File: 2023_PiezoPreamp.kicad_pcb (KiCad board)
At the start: 4 copper layers, 68 x 35.5 mm, 73 parts, among them J101 6.3mm stereo, J102 6.3mm stereo, J201 Molex PicoBlade, J301 2.54mm header, J401 Spring Contact, U101 OPA145, U102 OPA145, U201 ZXMP3A17E6TA, U301 MMDT2222A-7-F

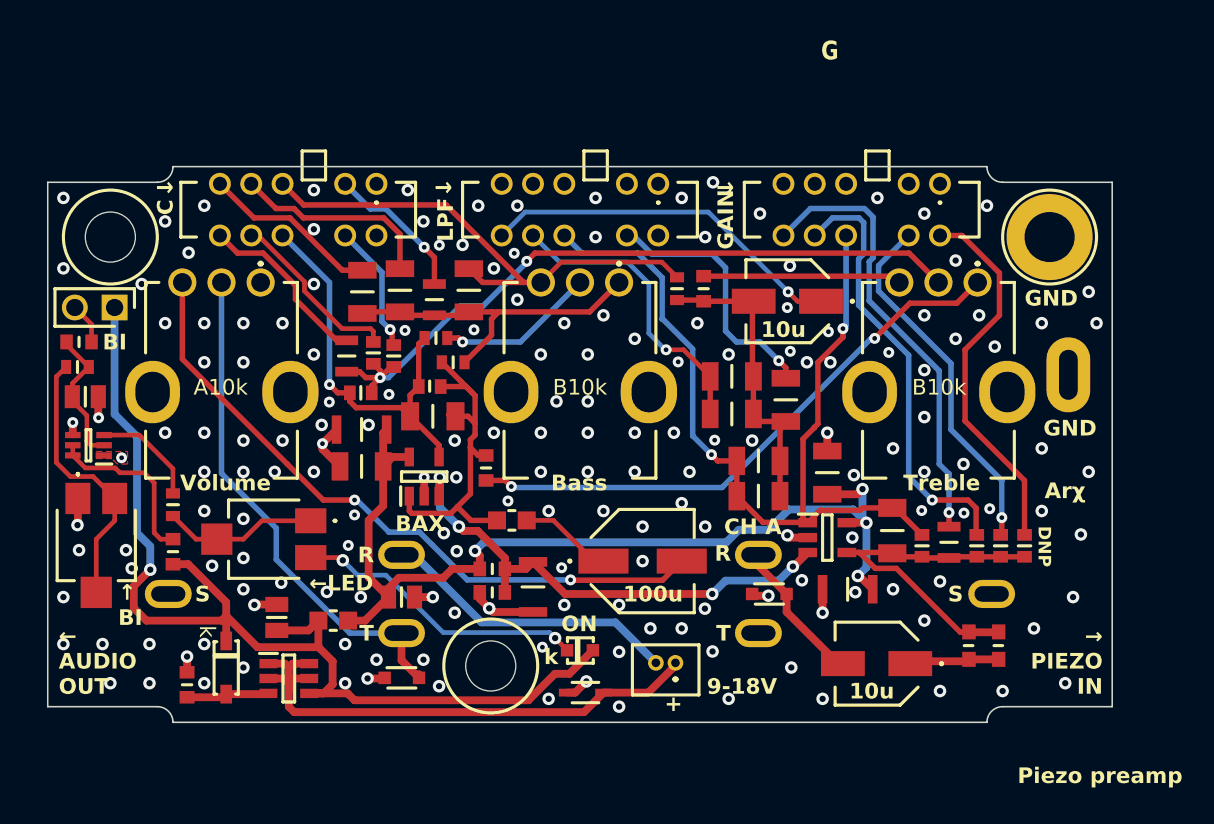
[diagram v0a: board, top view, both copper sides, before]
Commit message: resolving all violations of stitching vias
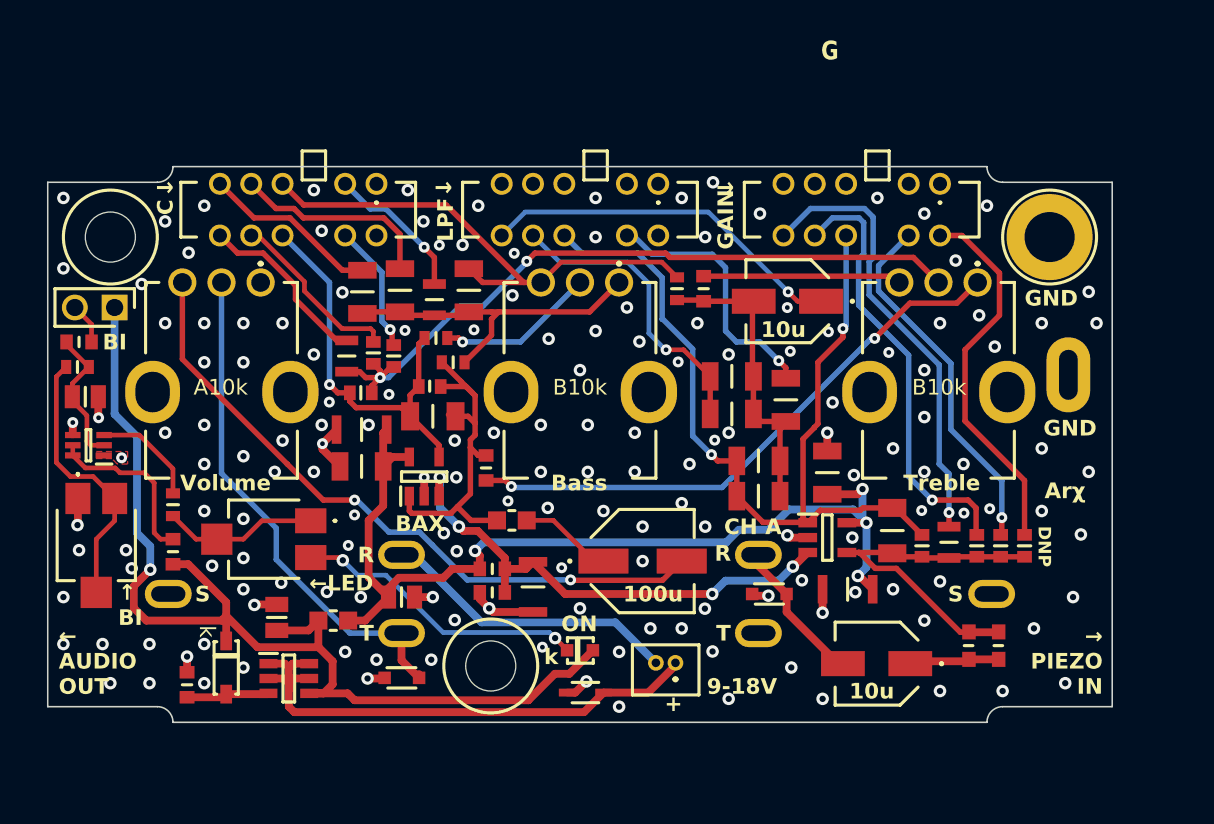
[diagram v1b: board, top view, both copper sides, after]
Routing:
- net GND: vias 177 -> 164
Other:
- board text removed: "Piezo preamp"

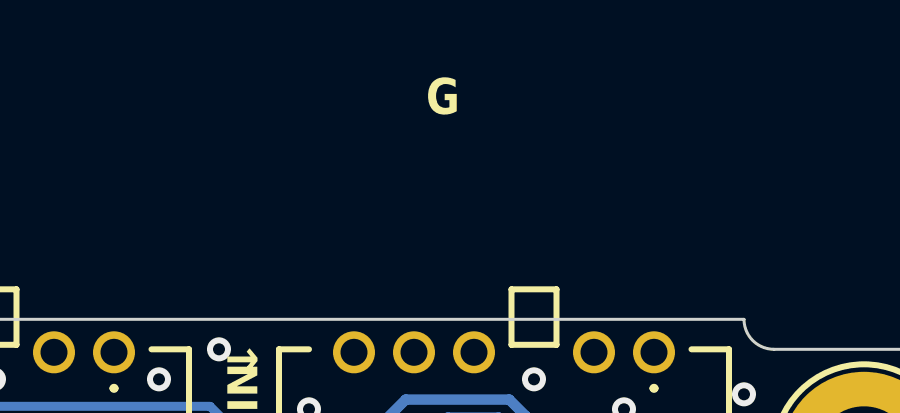
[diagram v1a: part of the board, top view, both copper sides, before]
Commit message: removing forggoten text
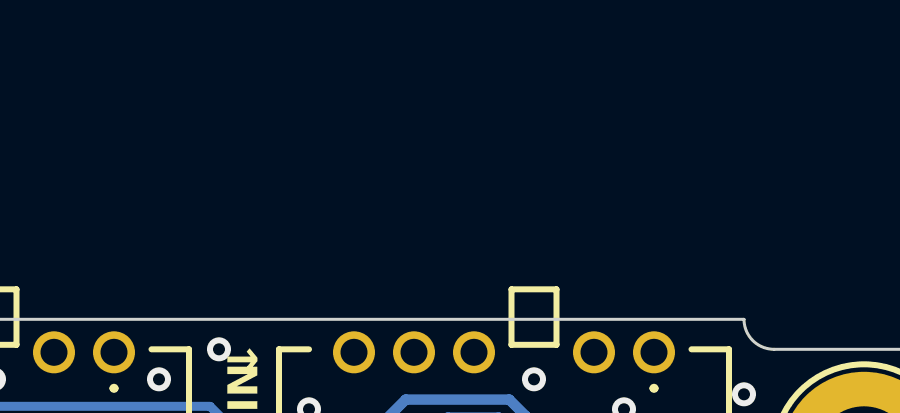
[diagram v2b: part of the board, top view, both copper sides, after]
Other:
- board text removed: "G"
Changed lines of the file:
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@@
     (effects (font (size 1 1) (thickness 0.2) bold) (justify left bottom))
-  )
-  (gr_text "G" (at 89.4 22.8) (layer "F.SilkS")
-    (effects (font (size 1.2 1) (thickness 0.2) bold) (justify left bottom))
   )
   (gr_text "DNP" (at 103.2 52.45 270) (layer "F.SilkS")

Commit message: final touches to board and schematic before manufacture / assembly
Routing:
- net /1-ChargeAmpAndEQ/CH_A_OUT: track 58.2 -> 57.3 mm
- net /1-ChargeAmpAndEQ/LPF_SW_6: track 23.9 -> 23.4 mm
- net GND: vias 164 -> 165
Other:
- board text added: "Arχ v2.0"
- board text added: "BAX↑"
- board text added: "BI↑"
- board text added: "CHA→"
- board text added: "JLCJLCJLCJLC"
- board text added: "L"
- board text added: "LOW"
- board text added: "NONE"
- board text added: "↑CENT"
- board text added: "↑GAIN"
- board text added: "↑LPF"
- board text added: "↖ BI"
- board text added: "↖LED"
- board text removed: "Arχ"
- board text removed: "BAX"
- board text removed: "BI"
- board text removed: "C"
- board text removed: "CH A"
- board text removed: "GAIN"
- board text removed: "LPF"
- board text removed: "←LED"
- board text removed: "↑ BI"
- board text removed: "→"

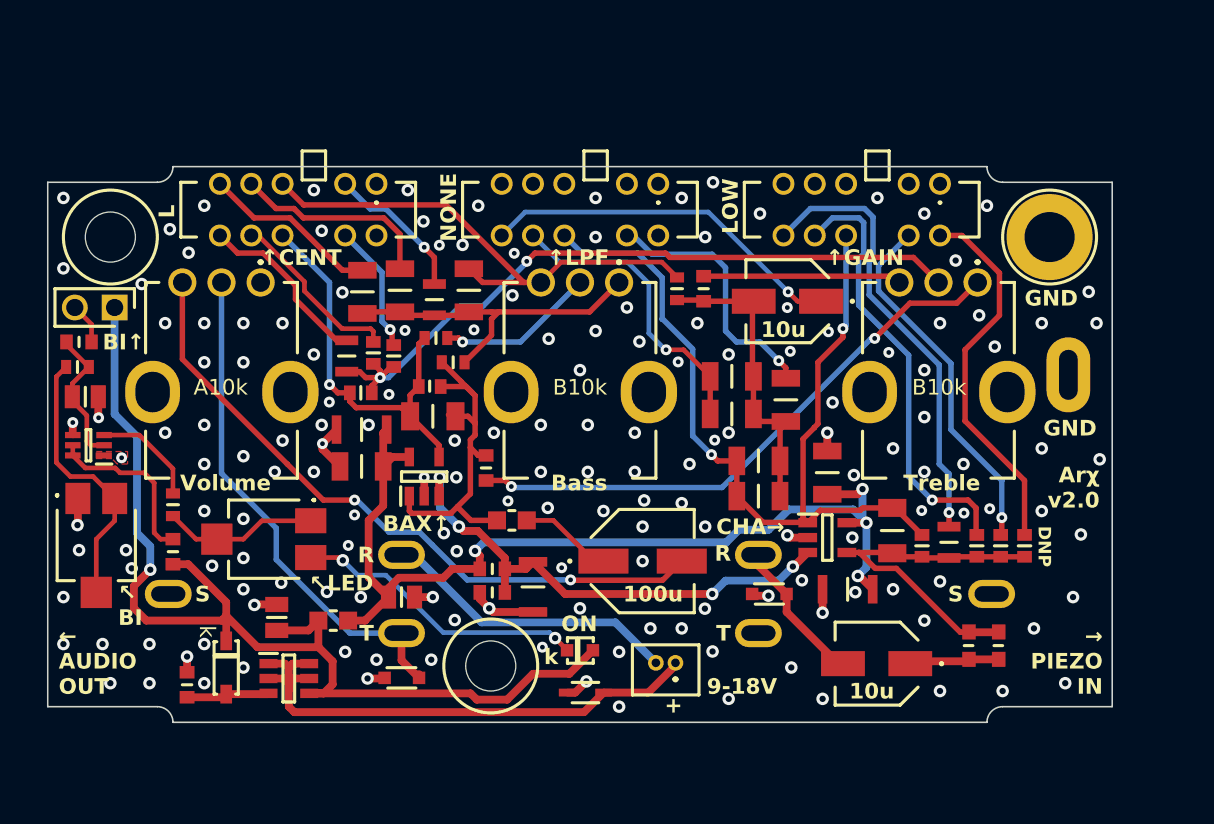
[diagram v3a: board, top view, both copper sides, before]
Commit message: fixing some of 0805 and 1206 land patterns so that they have enough soldering area (after JLC feedback)
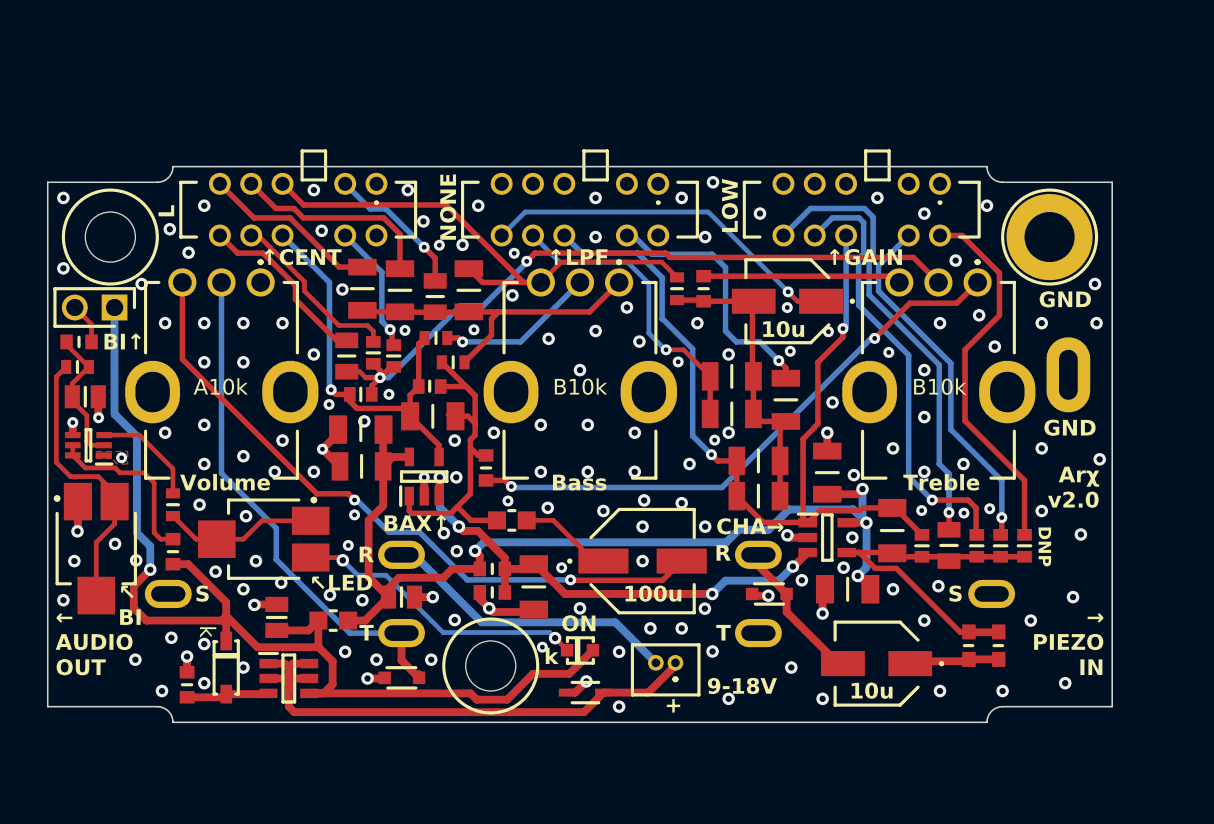
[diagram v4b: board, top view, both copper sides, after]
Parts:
- moved Cb104 0.21 mm to (64.8, 37.8)
- moved Cb102 0.20 mm to (60.1, 37.3)
- moved Cf102 0.20 mm to (97.6, 53.7)
- moved RV301 0.20 mm to (43.1, 53.9)
- moved Ct101 0.10 mm to (60.0, 44.0)
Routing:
- net GND: track 23.7 -> 24.0 mm, vias 165 -> 162

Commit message: PCB: few minor fixes, vias etc
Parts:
- D202: value DDZ12B-7 -> SOD3716X145N
- U201: value ZXMP3A17E6TA -> SOT95P285X140-6N
- U301: value MMDT2222A-7-F -> SOT65P210X110-6N
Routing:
- net Vbi: track 69.2 -> 61.0 mm
- net GND: vias 162 -> 175
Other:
- board text added: "Arχ v2.1"
- board text added: "↑ BI"
- board text added: "↑BI"
- board text removed: "Arχ v2.0"
- board text removed: "BI↑"
- board text removed: "↖ BI"

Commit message: updating the project and board (silkscreen mistake, was v2.0 instead of v2.1)
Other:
- board text added: "Piezo Preamp + EQ v2.1 12/2023 Arχ arx.wtf"
- board text removed: "Piezo Preamp + EQ v2.0 12/2023 Arχ arx.wtf"
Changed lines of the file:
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@@
     (effects (font (size 1 1) (thickness 0.2) bold) (justify left bottom mirror))
   )
-  (gr_text "Piezo Preamp + EQ \nv2.0 12/2023\nArχ\narx.wtf\n" (at 73.9 54.7) (layer "B.SilkS")
+  (gr_text "Piezo Preamp + EQ \nv2.1 12/2023\nArχ\narx.wtf\n" (at 73.9 54.7) (layer "B.SilkS")
     (effects (font (size 1.2 1) (thickness 0.2) bold) (justify bottom mirror))
   )

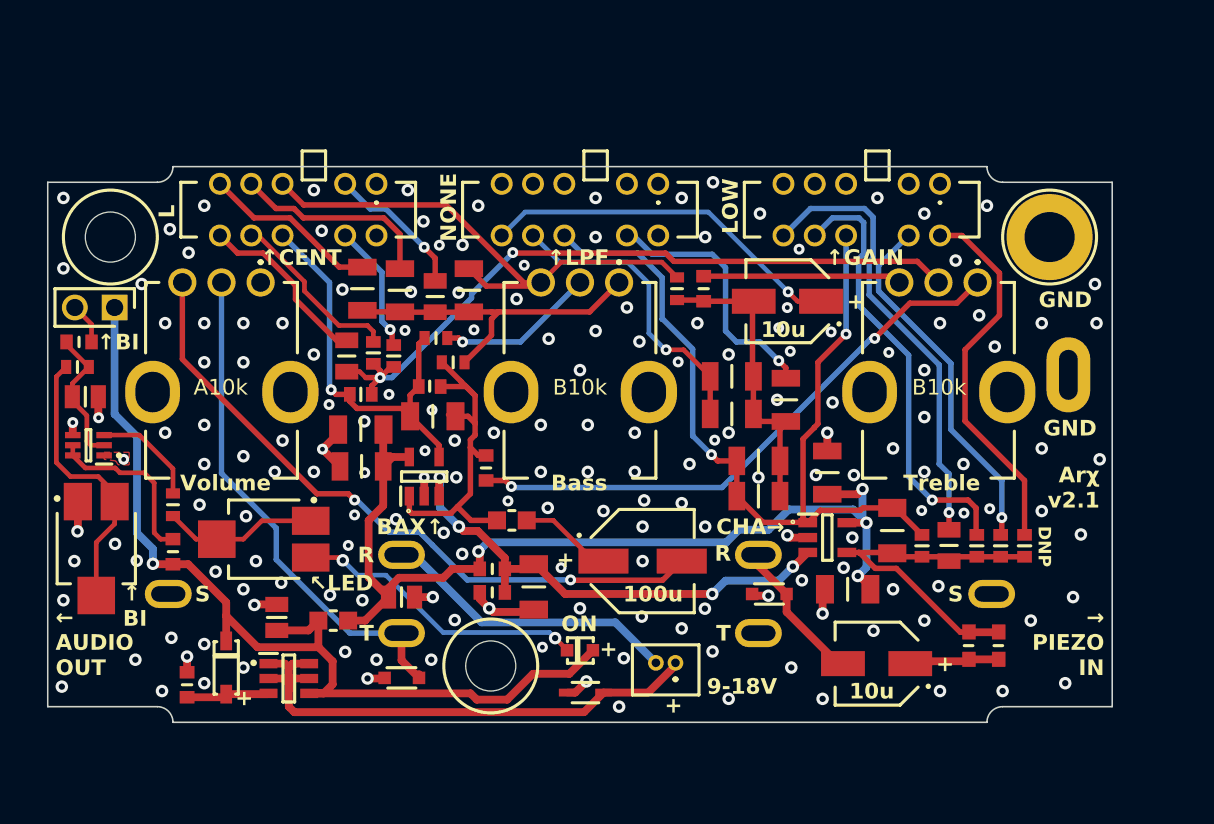
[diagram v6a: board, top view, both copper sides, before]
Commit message: v2.2: correcting pins of audio jacks - T and R were swapped. Fixing in schematic and PCB
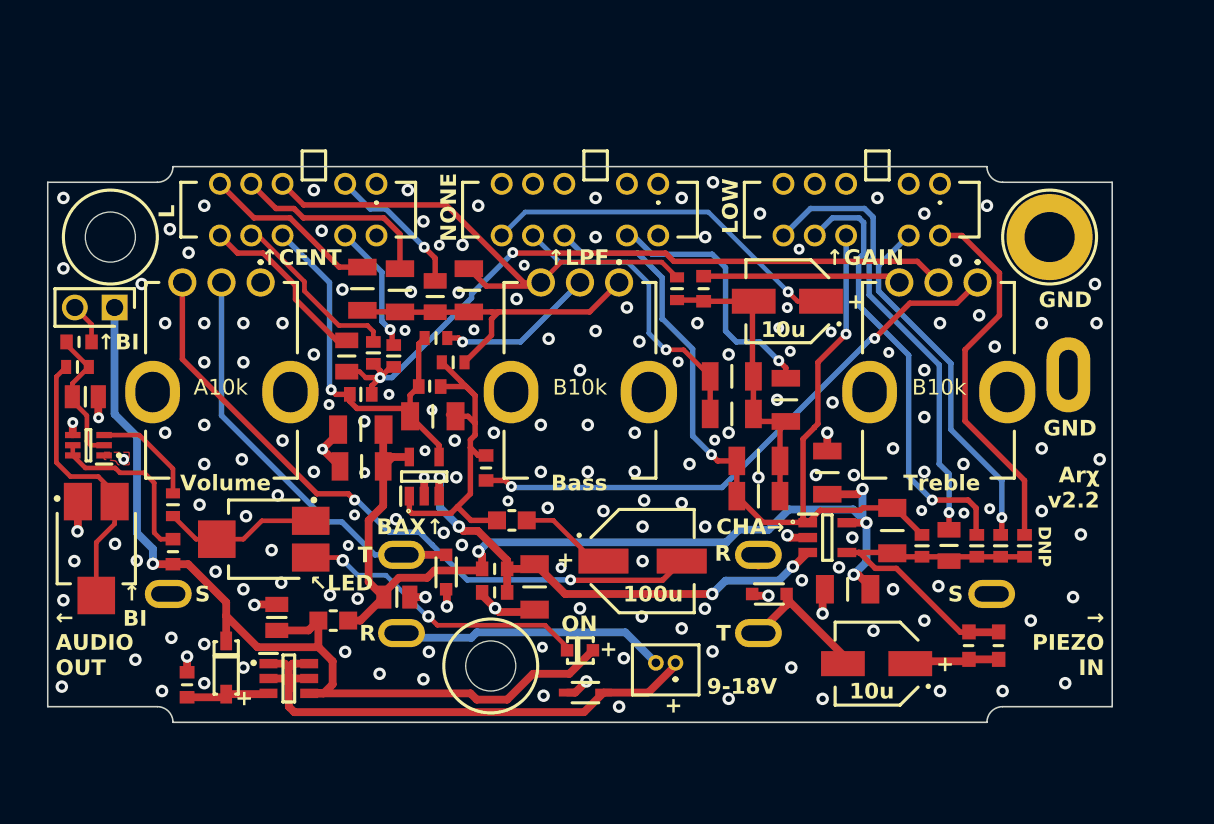
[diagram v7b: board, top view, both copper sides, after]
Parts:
- D202: value SOD3716X145N -> DDZ12B-7
- U201: value SOT95P285X140-6N -> ZXMP3A17E6TA
- U301: value SOT65P210X110-6N -> MMDT2222A-7-F
- moved D102 7.33 mm to (65.5, 55.4), turned to 90 degrees
- moved C202 0.30 mm to (62.3, 57.0)
- moved R203 0.15 mm to (68.5, 55.2)
- moved R204 0.15 mm to (68.5, 56.7)
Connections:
- J101 pad 2: GND -> /1-ChargeAmpAndEQ/PIEZO_IN
- J101 pad 3: /1-ChargeAmpAndEQ/PIEZO_IN -> GND
- J102 pad 2: DC_IN_NEG -> /1-ChargeAmpAndEQ/AUDIO_OUT
- J102 pad 3: /1-ChargeAmpAndEQ/AUDIO_OUT -> DC_IN_NEG
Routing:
- net /1-ChargeAmpAndEQ/AUDIO_OUT: track 32.7 -> 26.5 mm
- net DC_IN_NEG: track 19.1 -> 17.6 mm
- net GND: track 24.0 -> 24.3 mm, vias 175 -> 176
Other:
- board text added: "Arχ v2.2"
- board text added: "Piezo Preamp + EQ v2.2 12/2023 Arχ arx.wtf"
- board text removed: "Arχ v2.1"
- board text removed: "Piezo Preamp + EQ v2.1 12/2023 Arχ arx.wtf"

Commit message: v2.3: adjusting board dimensions to better fit Teko 1/A.1 enclosure. Increasing pad sizes for opamps and 10M resistors to make hand soldering easier.
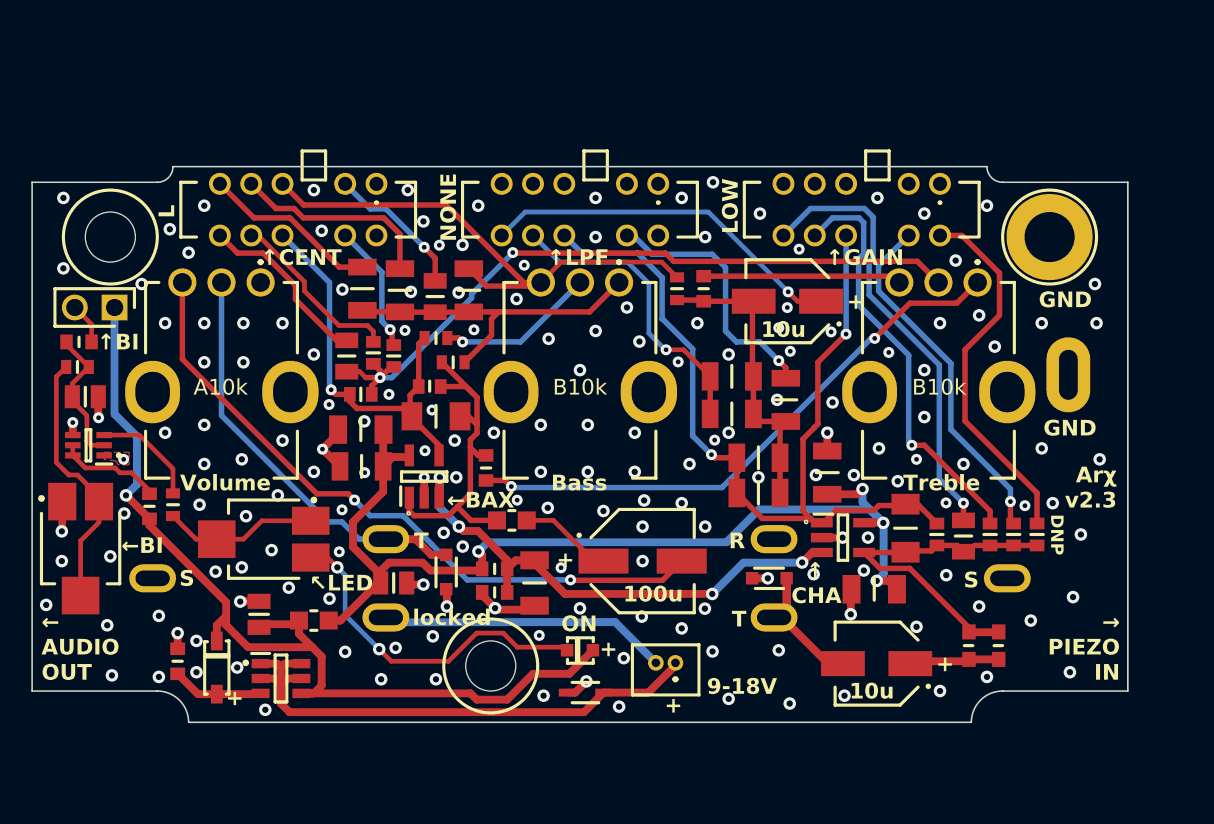
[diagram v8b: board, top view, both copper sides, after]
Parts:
- moved R303 3.26 mm to (46.5, 51.2)
- moved C205 1.70 mm to (92.8, 56.5)
- moved R201 1.62 mm to (48.3, 61.1)
- moved J101 1.41 mm to (101.3, 55.8)
- moved J102 1.41 mm to (46.7, 55.8)
- moved R202 1.24 mm to (57.0, 58.5)
- moved Cf101 1.20 mm to (96.8, 53.0)
- moved C201 1.15 mm to (53.5, 58.1)
- moved Cf103 1.12 mm to (100.2, 53.0)
- moved Cf102 1.10 mm to (98.5, 53.1)
- moved Cf104 1.10 mm to (101.7, 53.0)
- moved Cf105 1.08 mm to (103.2, 53.0)
- moved D101 1.00 mm to (86.1, 55.8)
- moved RV301 1.00 mm to (42.1, 53.9)
- moved U101 1.00 mm to (90.8, 53.2)
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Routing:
- net /3-BatteryIndicator/BI_B1: track 11.1 -> 6.68 mm
- net VS: track 62.2 -> 65.8 mm
- net /3-BatteryIndicator/LED_K: track 18.7 -> 21.7 mm
- net Vbias: track 32.2 -> 33.6 mm
- net /1-ChargeAmpAndEQ/PIEZO_IN: track 9.19 -> 10.5 mm
- net /1-ChargeAmpAndEQ/G_SW_7: track 28.3 -> 27.0 mm
- net GND: track 24.3 -> 23.1 mm
- net /3-BatteryIndicator/TRIM_BI_3: track 18.0 -> 16.8 mm
- net /1-ChargeAmpAndEQ/CH_A_OUT: track 57.3 -> 58.3 mm
- net DC_IN_NEG: track 17.6 -> 18.5 mm
- net /2-Power/DC_IN_POS: track 34.8 -> 35.7 mm
- net /2-Power/RP_GATE: track 5.30 -> 5.86 mm
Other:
- board size 68 x 35.5 mm -> 70 x 35.5 mm
- board text added: "Arχ v2.3"
- board text added: "Piezo Preamp + EQ v2.3 01/2024 Arχ arx.wtf"
- board text added: "locked"
- board text added: "←BAX"
- board text added: "←BI"
- board text added: "↑ CHA"
- board text removed: "Arχ v2.2"
- board text removed: "BAX↑"
- board text removed: "CHA→"
- board text removed: "Piezo Preamp + EQ v2.2 12/2023 Arχ arx.wtf"
- board text removed: "↑ BI"
